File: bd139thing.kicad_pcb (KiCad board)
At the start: 2 copper layers, 78 x 63 mm, 24 parts, among them J1 Audio-Jack-3, J2 Jack-DC, Q1 PN2222, Q2 BD13916, Q3 BD13916, Q4 PN2222, Q5 BD13916, Q6 BD13916

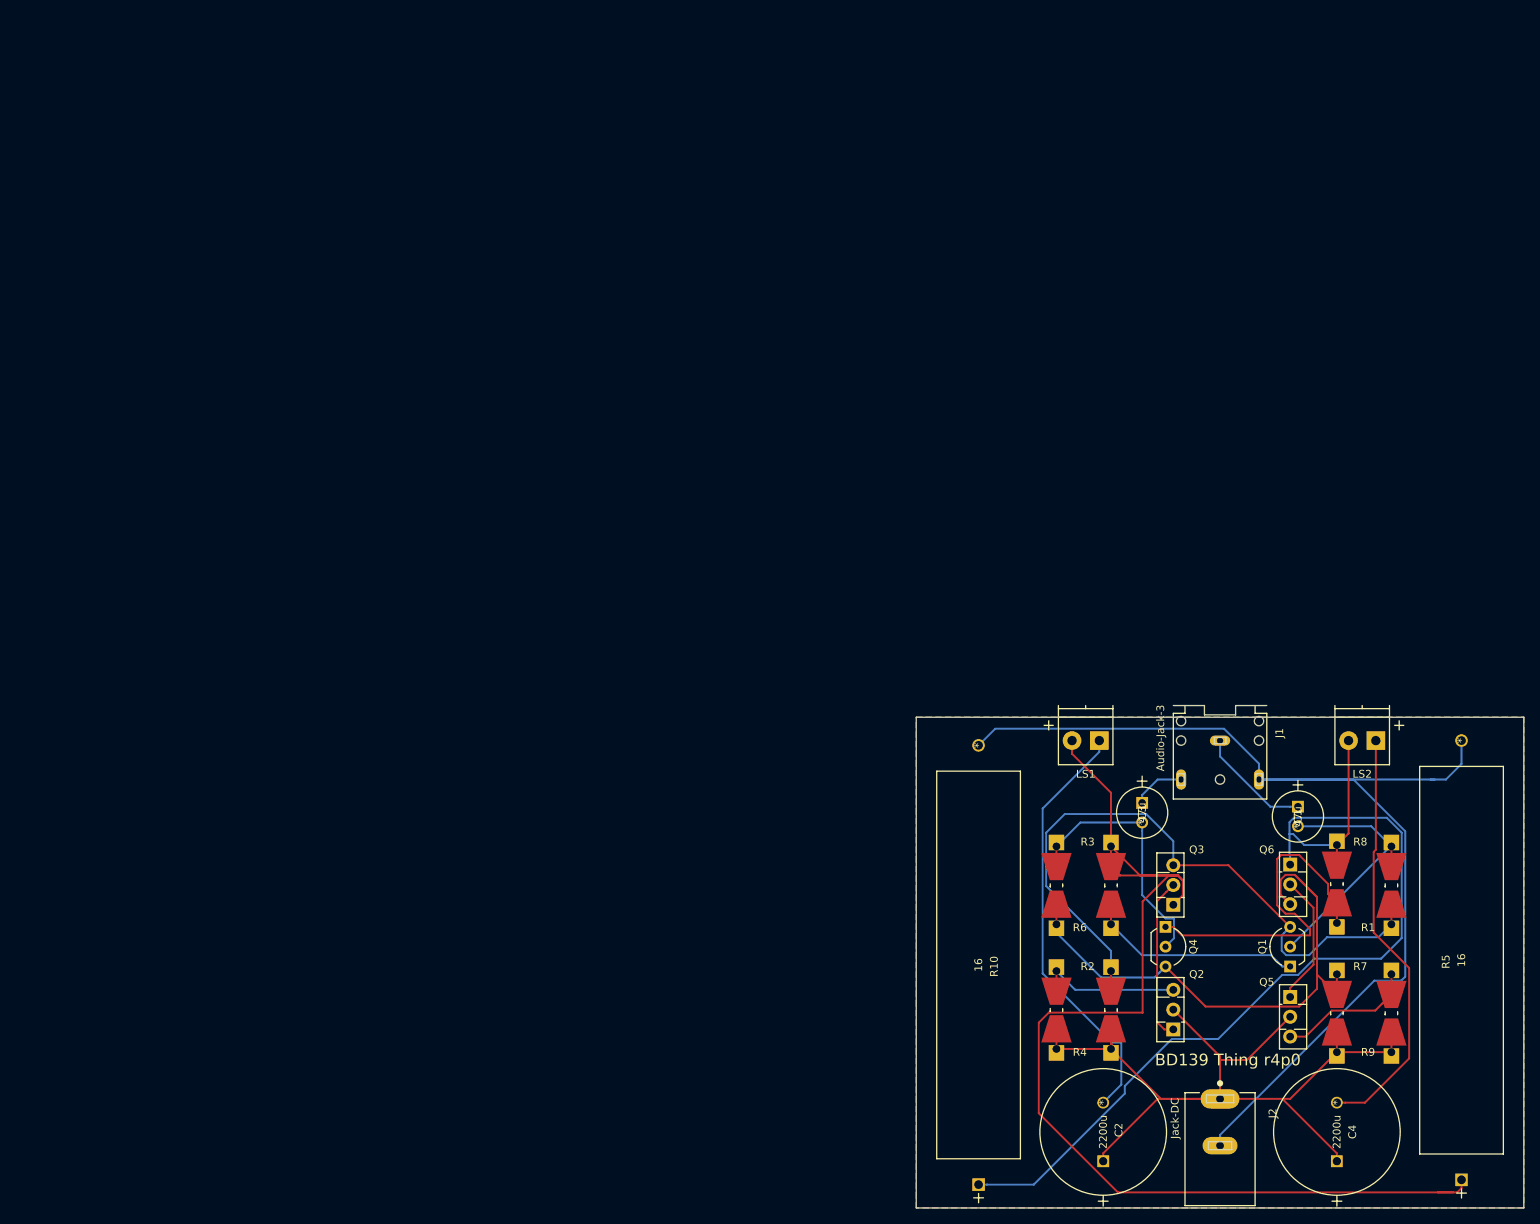
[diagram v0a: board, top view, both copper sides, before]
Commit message: r5p0 ok, improved placement on 75x75mm
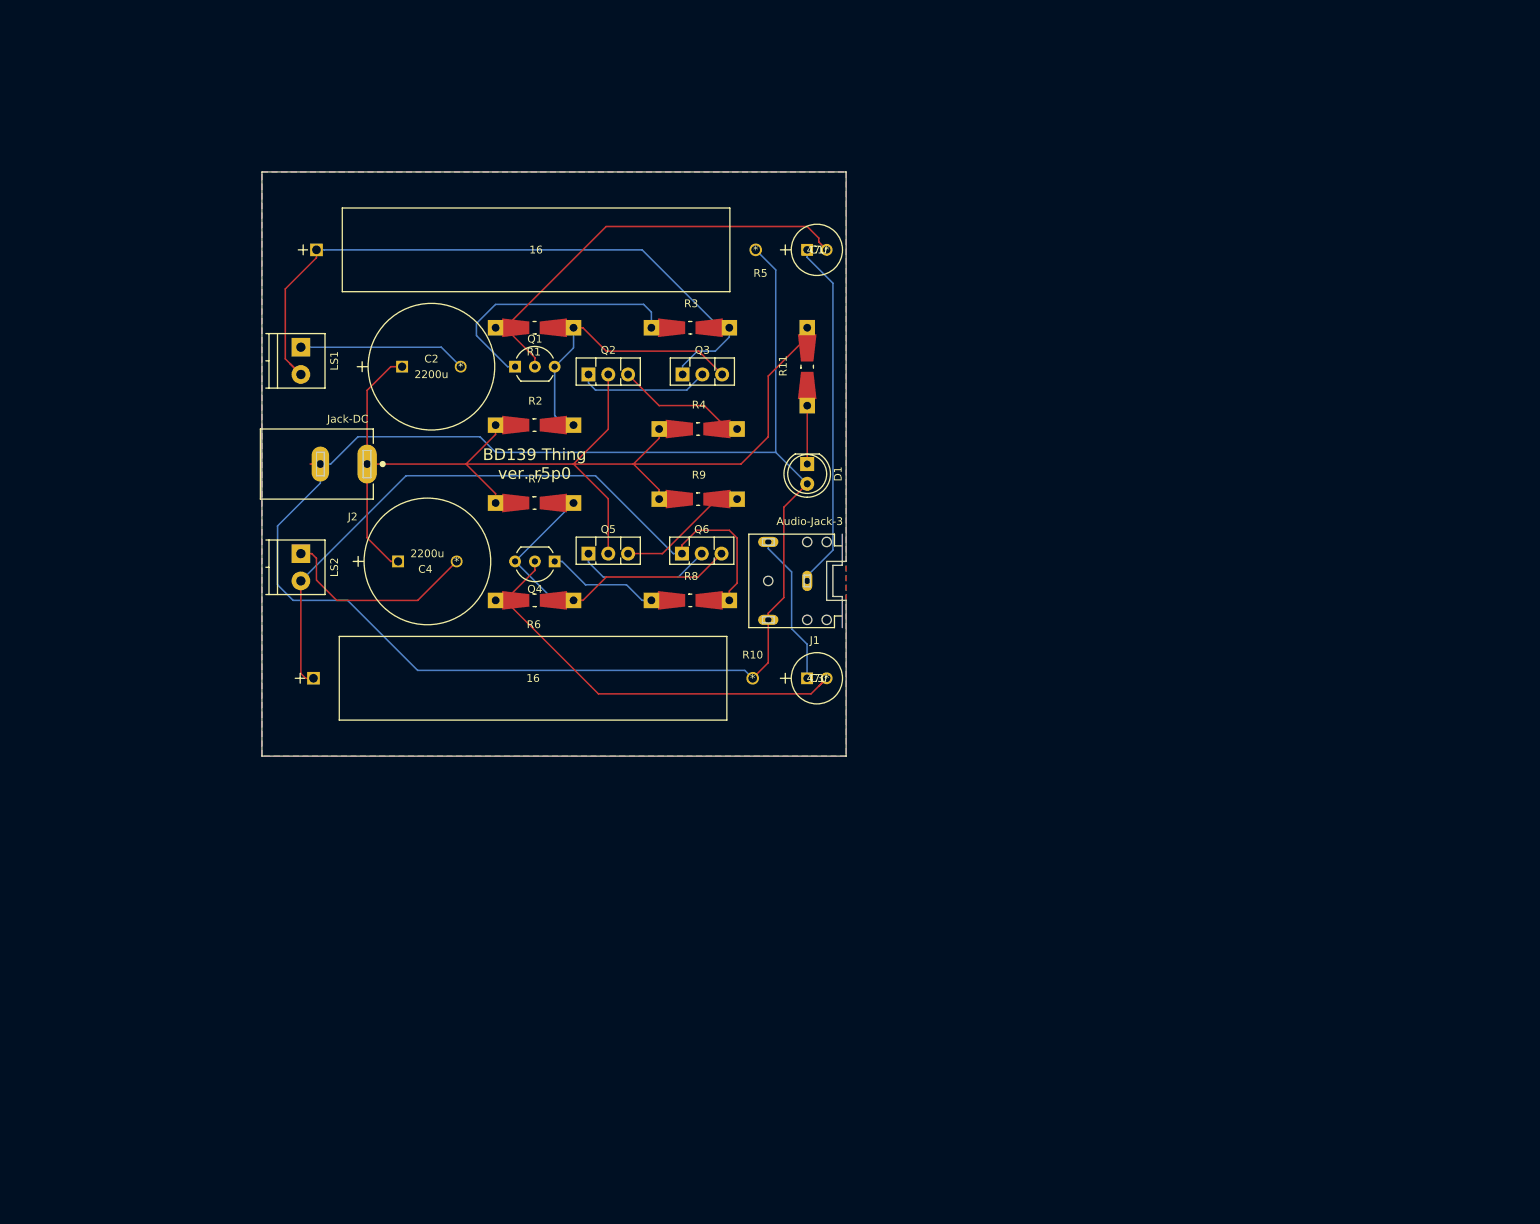
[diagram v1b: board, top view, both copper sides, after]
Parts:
- added D1: LED, LEDs:LED_D5.0mm, F.Cu at (100.0, 57.5)
- added R11: 10k, Resistors_Universal:Resistor_SMD+THTuniversal_0805to1206_RM10_HandSoldering, F.Cu at (100.0, 45.0)
- R1, R2, R3, R4, R6, R7, R8, R9: footprint Resistors_Universal:Resistor_SMD+THTuniversal_0805to2512_RM10_HandSoldering -> Resistors_Universal:Resistor_SMD+THTuniversal_0805to1206_RM10_HandSoldering
- moved LS2 140.1 mm to (35.0, 69.0), turned to 270 degrees
- moved J2 136.5 mm to (43.5, 57.5), turned to 180 degrees
- moved C4 132.7 mm to (55.0, 70.0), turned to 0 degrees
- moved R1 131.2 mm to (65.0, 40.0), turned to 180 degrees
- moved Q1 125.8 mm to (62.5, 45.0), turned to 0 degrees
- moved C2 125.4 mm to (55.5, 45.0), turned to 0 degrees
- moved R7 122.1 mm to (65.0, 62.5), turned to 0 degrees
- moved LS1 114.3 mm to (35.0, 42.5), turned to 270 degrees
- moved Q2 112.7 mm to (71.9, 46.0), turned to 0 degrees
- moved R9 110.8 mm to (86.0, 62.0), turned to 0 degrees
- moved R5 110.4 mm to (93.4, 30.0), turned to 0 degrees
- moved Q5 106.6 mm to (71.9, 69.0), turned to 0 degrees
- moved R2 105.4 mm to (65.0, 52.5), turned to 0 degrees
- moved C1 95.6 mm to (102.5, 30.0), turned to 0 degrees
- moved Q3 92.8 mm to (84.0, 46.0), turned to 0 degrees
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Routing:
- net Net-(LS1-Pad2): track 151.9 -> 90.5 mm
- net GND: track 145.0 -> 206.5 mm
- net Net-(Q1-Pad3): track 86.0 -> 41.9 mm
- net +12V: track 115.6 -> 159.0 mm
- net Net-(Q4-Pad3): track 84.9 -> 46.8 mm
- net Net-(LS2-Pad2): track 130.7 -> 92.8 mm
- net Net-(C2-Pad2): track 55.3 -> 21.6 mm
- net Net-(C1-Pad1): track 14.7 -> 45.2 mm
- net Net-(C4-Pad2): track 54.4 -> 26.2 mm
- net Net-(Q4-Pad1): track 45.0 -> 17.1 mm
- net Net-(C1-Pad2): track 34.0 -> 58.6 mm
- net Net-(C3-Pad2): track 33.5 -> 56.3 mm
- net Net-(C3-Pad1): track 6.84 -> 19.6 mm
- net Net-(D1-Pad1): track 0.00 -> 10.1 mm
- net Net-(Q1-Pad1): track 27.8 -> 36.6 mm
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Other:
- board size 78 x 63 mm -> 75 x 75 mm
- net class Default: clearance 0.2 -> 0.1; trace_width 0.25 -> 0.2; via_dia 0.6 -> 0.45
- rule trace_clearance: 0.2 -> 0.1
- board text added: "BD139 Thing ver. r5p0"
- board text removed: "+"
- board text removed: "BD139 Thing r4p0"

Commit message: prepare fixes p1
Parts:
- moved D1 2.50 mm to (100.0, 60.0), turned to 90 degrees
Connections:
- D1 pad 1: Net-(D1-Pad1) -> GND
- D1 pad 2: GND -> Net-(D1-Pad2)
- J1 pad 1: Net-(C1-Pad1) -> GND
- J1 pad 3: GND -> Net-(C1-Pad1)
- R11 pad 1: Net-(D1-Pad1) -> Net-(D1-Pad2)
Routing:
- net GND: track 206.5 -> 182.0 mm
- net Net-(C1-Pad1): track 45.2 -> 58.7 mm
- net Net-(D1-Pad1): track 10.1 -> 0.00 mm
- net Net-(D1-Pad2): track 0.00 -> 10.0 mm
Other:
- board text added: "BD139 Thing ver. r5p1"
- board text removed: "BD139 Thing ver. r5p0"
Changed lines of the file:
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@@
   (general
     (links 58)
-    (no_connects 0)
-    (area 17.650001 12.639345 105.831818 95.100001)
+    (no_connects 3)
+    (area 29.924999 19.924999 105.075001 95.075001)
     (thickness 1.6)
     (drawings 15)
-    (tracks 174)
+    (tracks 185)
     (zones 0)
     (modules 26)
@@
   (net 17 "Net-(Q5-Pad1)")
   (net 18 "Net-(Q5-Pad3)")
-  (net 19 "Net-(D1-Pad1)")
+  (net 19 "Net-(D1-Pad2)")
   (net_class Default "This is the default net class."
     (clearance 0.1)
@@
     (add_net "Net-(C3-Pad2)")
     (add_net "Net-(C4-Pad2)")
-    (add_net "Net-(D1-Pad1)")
+    (add_net "Net-(D1-Pad2)")
     (add_net "Net-(LS1-Pad2)")
     (add_net "Net-(LS2-Pad2)")
@@
     (fp_line (start -4.4 4.5) (end -3.5 4.5) (layer F.SilkS) (width 0.127))
     (pad 1 thru_hole oval (at 0 0 270) (size 2.616 1.308) (drill 0.8) (layers *.Cu *.Mask)
-      (net 1 "Net-(C1-Pad1)"))
+      (net 8 GND))
     (pad 2 thru_hole oval (at 5 5) (size 2.616 1.308) (drill 0.8) (layers *.Cu *.Mask)
       (net 5 "Net-(C3-Pad1)"))
     (pad 3 thru_hole oval (at 5 -5) (size 2.616 1.308) (drill 0.8) (layers *.Cu *.Mask)
-      (net 8 GND))
+      (net 1 "Net-(C1-Pad1)"))
     (pad Hole np_thru_hole circle (at -2.5 -5 180) (size 1.2 1.2) (drill 1.2) (layers *.Cu *.Mask F.SilkS))
     (pad Hole np_thru_hole circle (at 0 -5 180) (size 1.2 1.2) (drill 1.2) (layers *.Cu *.Mask F.SilkS))
@@
   )
   (module LEDs:LED_D5.0mm (layer F.Cu)
-    (at 100 57.5 270)
+    (at 100 60 90)
     (descr "LED, diameter 5.0mm, 2 pins, http://cdn-reichelt.de/documents/datenblatt/A500/LL-504BC2E-009.pdf")
     (tags "LED diameter 5.0mm 2 pins")
-    (fp_text reference D1 (at 1.27 -3.96 270) (layer F.SilkS)
-      (effects (font (size 1 1) (thickness 0.15)))
-    )
-    (fp_text value LED (at 1.27 3.96 270) (layer F.Fab)
+    (fp_text reference D1 (at 1.27 -3.96 90) (layer F.SilkS)
+      (effects (font (size 1 1) (thickness 0.15)))
+    )
+    (fp_text value LED (at 1.27 3.96 90) (layer F.Fab)
       (effects (font (size 1 1) (thickness 0.15)))
     )
@@
     (fp_line (start 4.5 3.25) (end 4.5 -3.25) (layer F.CrtYd) (width 0.05))
     (fp_line (start 4.5 -3.25) (end -1.95 -3.25) (layer F.CrtYd) (width 0.05))
-    (fp_text user %R (at 1.25 0 270) (layer F.Fab)
+    (fp_text user %R (at 1.25 0 90) (layer F.Fab)
       (effects (font (size 0.8 0.8) (thickness 0.2)))
     )
-    (pad 1 thru_hole rect (at 0 0 270) (size 1.8 1.8) (drill 0.9) (layers *.Cu *.Mask)
-      (net 19 "Net-(D1-Pad1)"))
-    (pad 2 thru_hole circle (at 2.54 0 270) (size 1.8 1.8) (drill 0.9) (layers *.Cu *.Mask)
+    (pad 1 thru_hole rect (at 0 0 90) (size 1.8 1.8) (drill 0.9) (layers *.Cu *.Mask)
       (net 8 GND))
+    (pad 2 thru_hole circle (at 2.54 0 90) (size 1.8 1.8) (drill 0.9) (layers *.Cu *.Mask)
+      (net 19 "Net-(D1-Pad2)"))
     (model ${KISYS3DMOD}/LEDs.3dshapes/LED_D5.0mm.wrl
       (at (xyz 0 0 0))
@@
     (descr "Resistor, SMD and THT, universal, 0805 to 1206,RM10,  Hand soldering,")
     (tags "Resistor, SMD and THT, universal, 0805 to 1206, RM10, Hand soldering,")
-    (fp_text reference R1 (at 0.09906 -3.0988 180) (layer F.SilkS)
+    (fp_text reference R1 (at -0.00126 2.5 180) (layer F.SilkS)
       (effects (font (size 1 1) (thickness 0.15)))
     )
@@
     (descr "Resistor, SMD and THT, universal, 0805 to 1206,RM10,  Hand soldering,")
     (tags "Resistor, SMD and THT, universal, 0805 to 1206, RM10, Hand soldering,")
-    (fp_text reference R7 (at 0.09906 -3.0988) (layer F.SilkS)
+    (fp_text reference R7 (at 0.00126 2.5) (layer F.SilkS)
       (effects (font (size 1 1) (thickness 0.15)))
     )
@@
     (fp_line (start -0.20066 -0.8001) (end 0.20066 -0.8001) (layer F.SilkS) (width 0.15))
     (pad 1 smd trapezoid (at -2.413 0 90) (size 3.50012 1.99898) (rect_delta 0.39878 0 ) (layers F.Cu F.Paste F.Mask)
-      (net 19 "Net-(D1-Pad1)"))
+      (net 19 "Net-(D1-Pad2)"))
     (pad 2 smd trapezoid (at 2.413 0 270) (size 3.50012 1.99898) (rect_delta 0.39878 0 ) (layers F.Cu F.Paste F.Mask)
       (net 3 +12V))
     (pad 1 thru_hole rect (at -5.00126 0 270) (size 1.99898 1.99898) (drill 1.00076) (layers *.Cu *.Mask)
-      (net 19 "Net-(D1-Pad1)"))
+      (net 19 "Net-(D1-Pad2)"))
     (pad 2 thru_hole rect (at 5.00126 0 270) (size 1.99898 1.99898) (drill 1.00076) (layers *.Cu *.Mask)
       (net 3 +12V))
   )
-  (gr_text "BD139 Thing\nver. r5p0" (at 65 57.5) (layer F.SilkS)
+  (gr_text "BD139 Thing\nver. r5p1" (at 65 57.5) (layer F.SilkS)
     (effects (font (size 1.5 1.5) (thickness 0.3)))
   )
@@
   )
   (segment (start 99.9854 30) (end 99.9854 30.962) (width 0.2) (layer B.Cu) (net 1))
-  (segment (start 99.9854 30.962) (end 103.300001 34.276601) (width 0.2) (layer B.Cu) (net 1))
-  (segment (start 103.300001 34.276601) (end 103.300001 68.545999) (width 0.2) (layer B.Cu) (net 1))
-  (segment (start 103.300001 68.545999) (end 100 71.846) (width 0.2) (layer B.Cu) (net 1))
-  (segment (start 100 71.846) (end 100 72.5) (width 0.2) (layer B.Cu) (net 1))
+  (segment (start 95 76.646) (end 95 77.5) (width 0.2) (layer B.Cu) (net 1))
+  (segment (start 99.9854 30.962) (end 102.5 33.4766) (width 0.2) (layer B.Cu) (net 1))
+  (segment (start 92.5 74.146) (end 95 76.646) (width 0.2) (layer B.Cu) (net 1))
+  (segment (start 102.5 33.4766) (end 102.5 64.584) (width 0.2) (layer B.Cu) (net 1))
+  (segment (start 102.5 64.584) (end 102.084 65) (width 0.2) (layer B.Cu) (net 1))
+  (segment (start 102.084 65) (end 95 65) (width 0.2) (layer B.Cu) (net 1))
+  (segment (start 92.5 67.5) (end 92.5 74.146) (width 0.2) (layer B.Cu) (net 1))
+  (segment (start 95 65) (end 92.5 67.5) (width 0.2) (layer B.Cu) (net 1))
+  (segment (start 95 76.646) (end 95 77.5) (width 0.2) (layer F.Cu) (net 1))
   (segment (start 62.58574 40) (end 59.99748 40) (width 0.2) (layer F.Cu) (net 2))
   (segment (start 59.99748 40) (end 61.19697 40) (width 0.2) (layer F.Cu) (net 2))
@@
   (segment (start 37 69.6) (end 36.4 69) (width 0.2) (layer F.Cu) (net 7))
   (segment (start 36.4 69) (end 35 69) (width 0.2) (layer F.Cu) (net 7))
-  (segment (start 95.96 56) (end 95.96 32.572) (width 0.2) (layer B.Cu) (net 8))
+  (segment (start 103.300001 68.545999) (end 100 71.846) (width 0.2) (layer B.Cu) (net 8))
+  (segment (start 93.388 30) (end 93.388 54.488) (width 0.2) (layer B.Cu) (net 8))
+  (segment (start 93.388 54.488) (end 98.9 60) (width 0.2) (layer B.Cu) (net 8))
+  (segment (start 98.9 60) (end 100 60) (width 0.2) (layer B.Cu) (net 8))
+  (segment (start 97.5 77.5) (end 100 75) (width 0.2) (layer F.Cu) (net 8))
+  (segment (start 100 75) (end 100 72.5) (width 0.2) (layer F.Cu) (net 8))
+  (segment (start 97.5 82.5) (end 97.5 77.5) (width 0.2) (layer F.Cu) (net 8))
+  (segment (start 95 85) (end 97.5 82.5) (width 0.2) (layer F.Cu) (net 8))
+  (segment (start 93 85) (end 95 85) (width 0.2) (layer F.Cu) (net 8))
+  (segment (start 100 60) (end 100 61.1) (width 0.2) (layer F.Cu) (net 8))
+  (segment (start 100 61.1) (end 99.146 61.954) (width 0.2) (layer F.Cu) (net 8))
+  (segment (start 99.146 61.954) (end 99.146 70.992) (width 0.2) (layer F.Cu) (net 8))
+  (segment (start 99.146 70.992) (end 100 71.846) (width 0.2) (layer F.Cu) (net 8))
+  (segment (start 100 71.846) (end 100 72.5) (width 0.2) (layer F.Cu) (net 8))
+  (segment (start 100 71.846) (end 100 72.5) (width 0.2) (layer B.Cu) (net 8))
   (segment (start 95.96 32.572) (end 93.388 30) (width 0.2) (layer B.Cu) (net 8))
   (segment (start 37.5 57.5) (end 38.825 57.5) (width 0.2) (layer B.Cu) (net 8))
-  (segment (start 60 56) (end 95.96 56) (width 0.2) (layer B.Cu) (net 8))
   (segment (start 38.825 57.5) (end 42.325 54) (width 0.2) (layer B.Cu) (net 8))
   (segment (start 42.325 54) (end 58 54) (width 0.2) (layer B.Cu) (net 8))
-  (segment (start 95.96 56) (end 100 60.04) (width 0.2) (layer B.Cu) (net 8))
   (segment (start 58 54) (end 60 56) (width 0.2) (layer B.Cu) (net 8))
   (segment (start 93 85) (end 91.987199 83.987199) (width 0.2) (layer B.Cu) (net 8))
@@
   (segment (start 32 65.45) (end 37.5 59.95) (width 0.2) (layer B.Cu) (net 8))
   (segment (start 37.5 59.95) (end 37.5 57.5) (width 0.2) (layer B.Cu) (net 8))
-  (segment (start 95 77.5) (end 95 83) (width 0.2) (layer F.Cu) (net 8))
-  (segment (start 95 83) (end 93 85) (width 0.2) (layer F.Cu) (net 8))
   (segment (start 36.175 57.5) (end 37.5 57.5) (width 0.2) (layer F.Cu) (net 8))
-  (segment (start 100 60.04) (end 97 63.04) (width 0.2) (layer F.Cu) (net 8))
-  (segment (start 97 63.04) (end 97 74.646) (width 0.2) (layer F.Cu) (net 8))
-  (segment (start 97 74.646) (end 95 76.646) (width 0.2) (layer F.Cu) (net 8))
-  (segment (start 95 76.646) (end 95 77.5) (width 0.2) (layer F.Cu) (net 8))
   (segment (start 90 40) (end 87.41174 40) (width 0.2) (layer F.Cu) (net 9))
   (segment (start 90 40) (end 88.80051 40) (width 0.2) (layer B.Cu) (net 9))
@@
   (segment (start 77 69) (end 81.41174 69) (width 0.2) (layer F.Cu) (net 18))
   (segment (start 81.41174 69) (end 88.41174 62) (width 0.2) (layer F.Cu) (net 18))
+  (segment (start 100 50) (end 100 57.46) (width 0.2) (layer F.Cu) (net 19))
   (segment (start 100 50) (end 100 47.41174) (width 0.2) (layer F.Cu) (net 19))
-  (segment (start 100 57.5) (end 100 50) (width 0.2) (layer F.Cu) (net 19))
   (zone (net 8) (net_name GND) (layer F.Cu) (hatch edge 0.508)
     (connect_pads (clearance 0.508))
